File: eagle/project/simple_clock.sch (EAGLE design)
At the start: 7 parts, among them IC1 MAX7219CNG

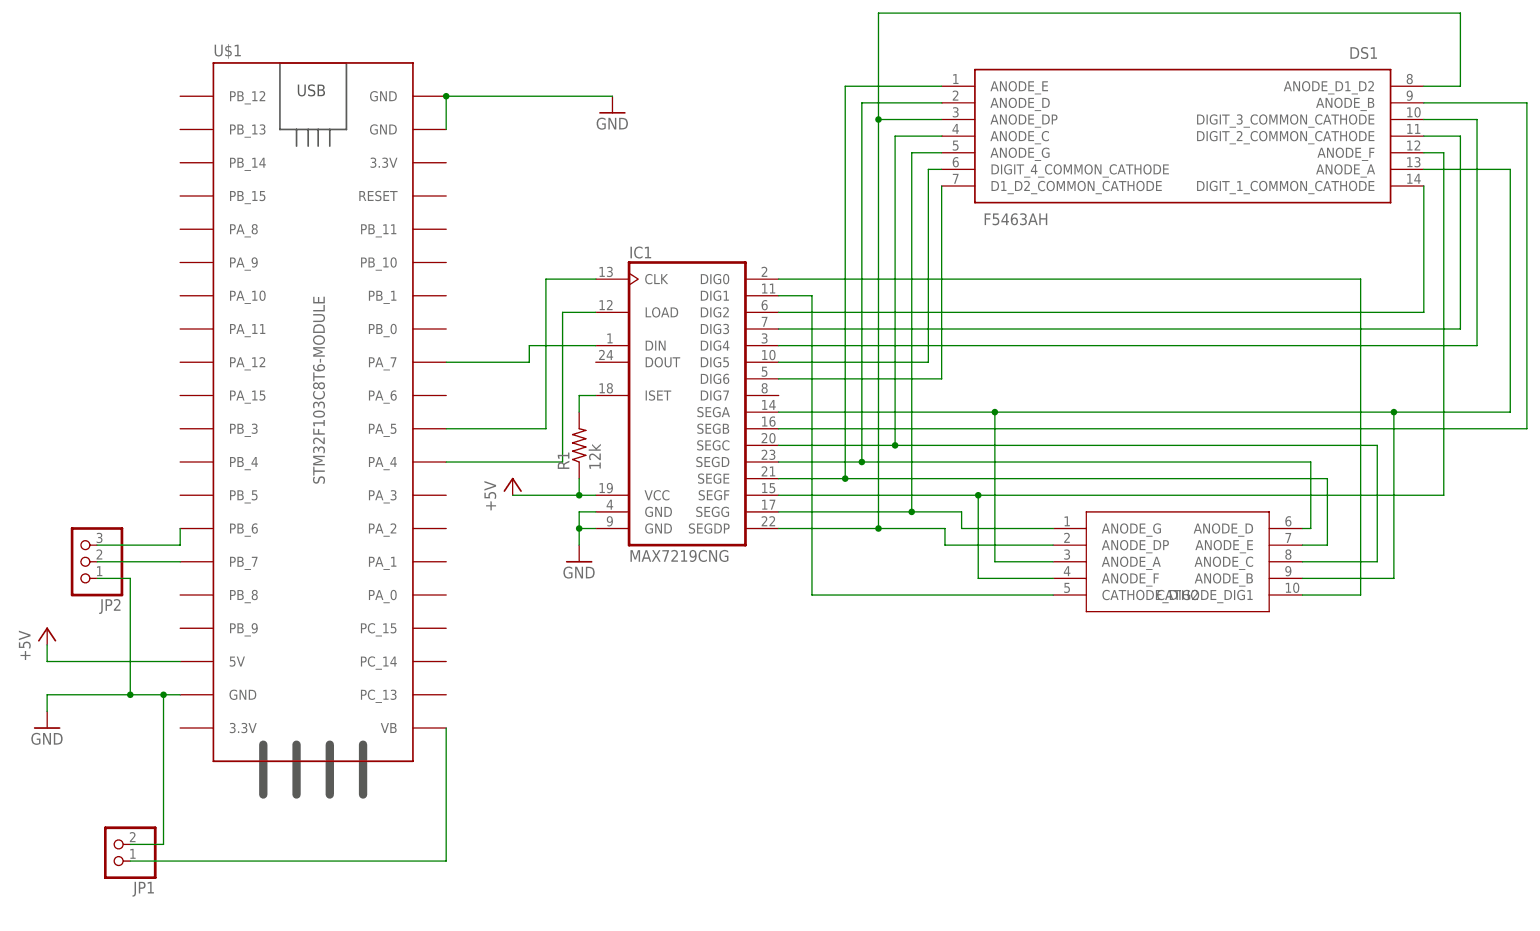
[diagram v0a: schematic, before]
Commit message: made pcb in Eagle
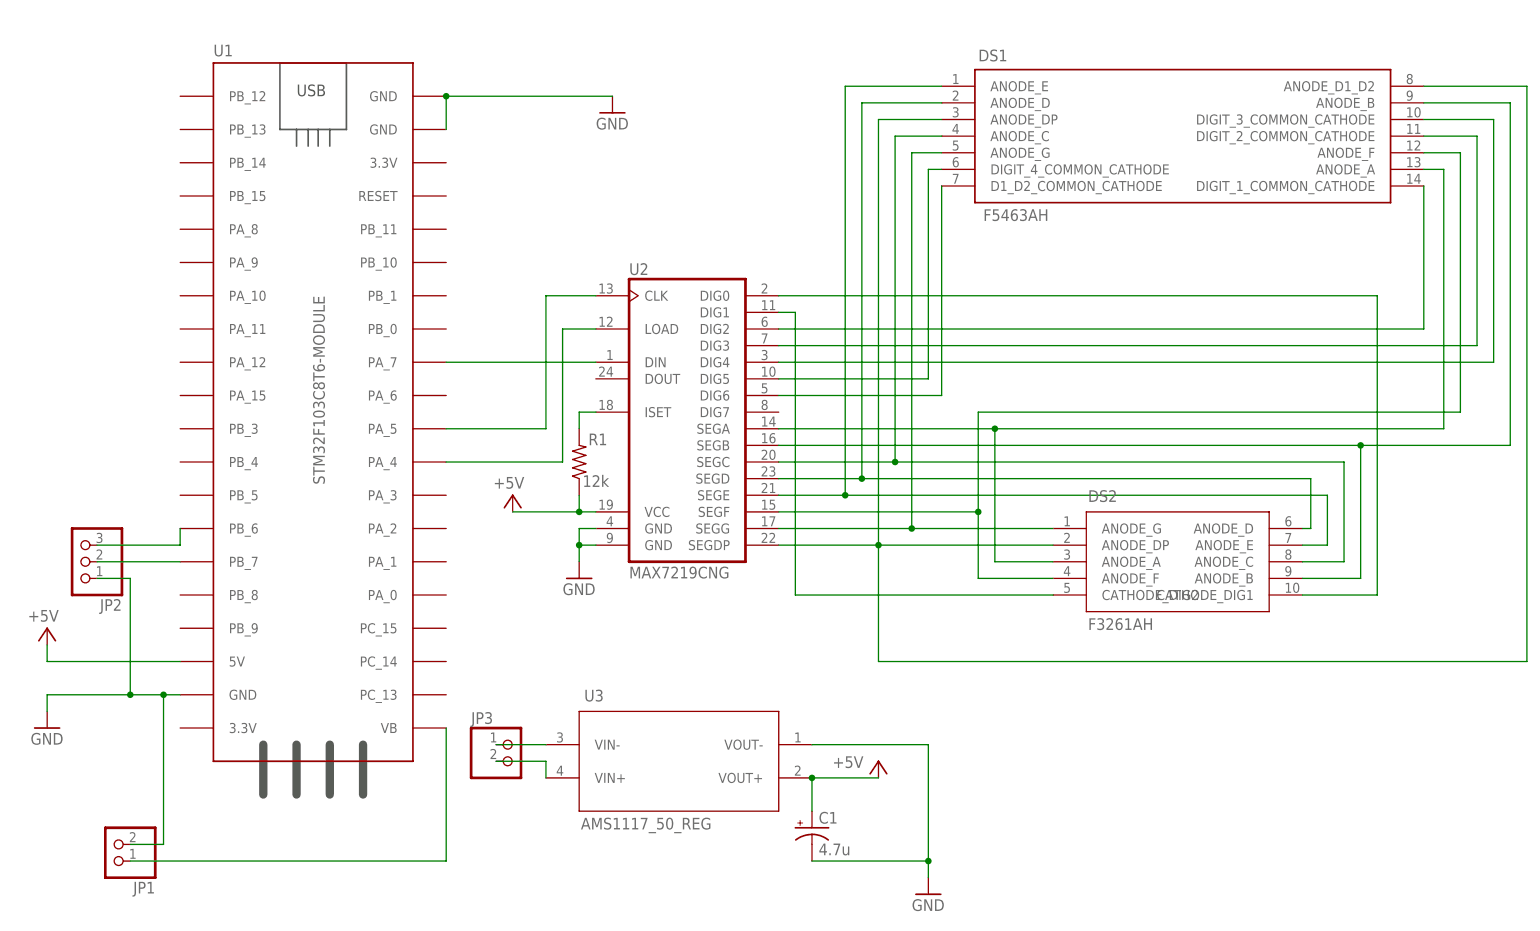
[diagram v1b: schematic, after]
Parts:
- removed IC1: MAX7219CNG, maxim:MAX7219CNG
- removed U$2: F3261AH, clock-7-seg:F3261AH
- added C1: 4.7u, rcl:CPOL-USE1.8-4
- added DS2: F3261AH, simple_clock:F3261AH
- added JP3: (no value), pinhead:PINHD-1X2
- added U2: MAX7219CNG, maxim:MAX7219CNG
- added U3: AMS1117_50_REG, simple_clock:AMS1117_50_REG
- DS1: device clock-7-seg:F5463AH -> simple_clock:F5463AH
- renumbered U$1 to U1
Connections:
- removed net N$17: DS1.ANODE_D1_D2, DS1.ANODE_DP, IC1.SEGDP, U$2.ANODE_DP
- new net N$23: JP3.1, U3.VIN-
- new net N$24: JP3.2, U3.VIN+
- new net N$25: DS1.ANODE_B, DS2.ANODE_B, U2.SEGB
- net +5V: now also C1.+, U2.VCC, U3.VOUT+; no longer IC1.VCC
- net GND: now also C1.-, U2.GND@1, U2.GND@2, U3.VOUT-; no longer IC1.GND@1, IC1.GND@2
- net N$1: now also U2.DIG4; no longer IC1.DIG4
- net N$10: now also U2.LOAD; no longer IC1.LOAD
- net N$11: now also DS2.ANODE_A, U2.SEGA; no longer IC1.SEGA, U$2.ANODE_A, U$2.ANODE_B
- net N$12: now also DS2.ANODE_E, U2.SEGE; no longer IC1.SEGE, U$2.ANODE_E
- net N$13: now also DS1.ANODE_D1_D2, DS1.ANODE_DP, DS2.ANODE_DP, U2.SEGDP; no longer DS1.ANODE_B, IC1.SEGB
- net N$14: now also DS2.ANODE_F, U2.SEGF; no longer IC1.SEGF, U$2.ANODE_F
- net N$15: now also DS2.ANODE_C, U2.SEGC; no longer IC1.SEGC, U$2.ANODE_C
- net N$16: now also DS2.ANODE_D, U2.SEGD; no longer IC1.SEGD, U$2.ANODE_D
- net N$18: now also DS2.ANODE_G, U2.SEGG; no longer IC1.SEGG, U$2.ANODE_G
- net N$19: now also U2.ISET; no longer IC1.ISET
- net N$2: now also U2.DIG6; no longer IC1.DIG6
- net N$3: now also U2.DIN; no longer IC1.DIN
- net N$4: now also U2.DIG2; no longer IC1.DIG2
- net N$5: now also DS2.CATHODE_DIG1, U2.DIG0; no longer IC1.DIG0, U$2.CATHODE_DIG1
- net N$6: now also DS2.CATHODE_DIG2, U2.DIG1; no longer IC1.DIG1, U$2.CATHODE_DIG2
- net N$7: now also U2.DIG3; no longer IC1.DIG3
- net N$8: now also U2.DIG5; no longer IC1.DIG5
- net N$9: now also U2.CLK; no longer IC1.CLK
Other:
- moved on the sheet: R1

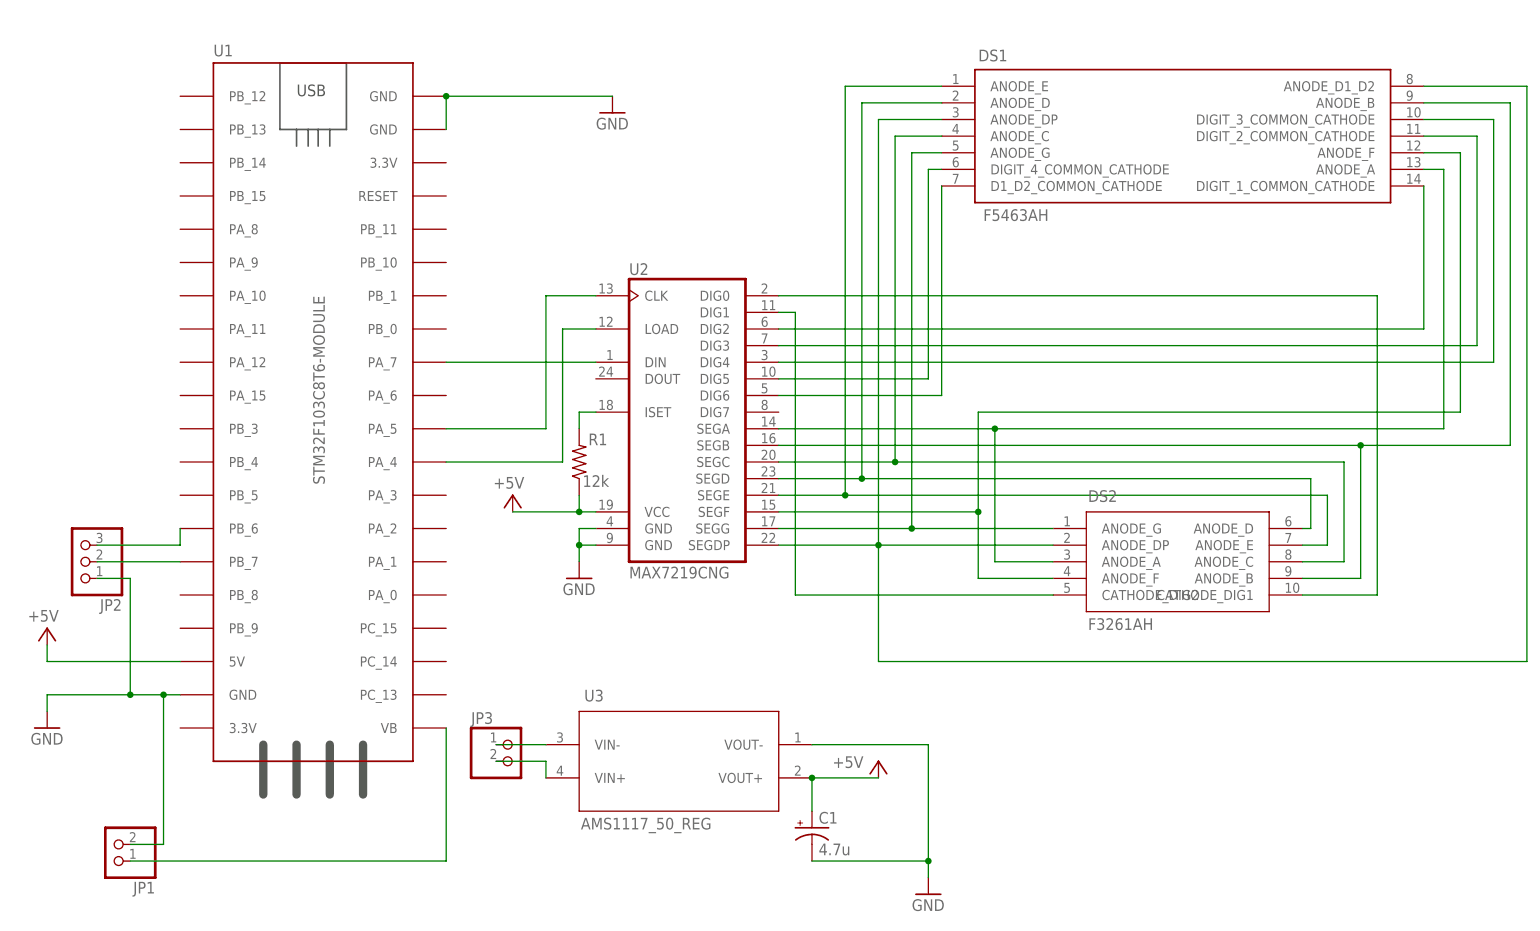
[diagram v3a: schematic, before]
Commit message: updated footprints
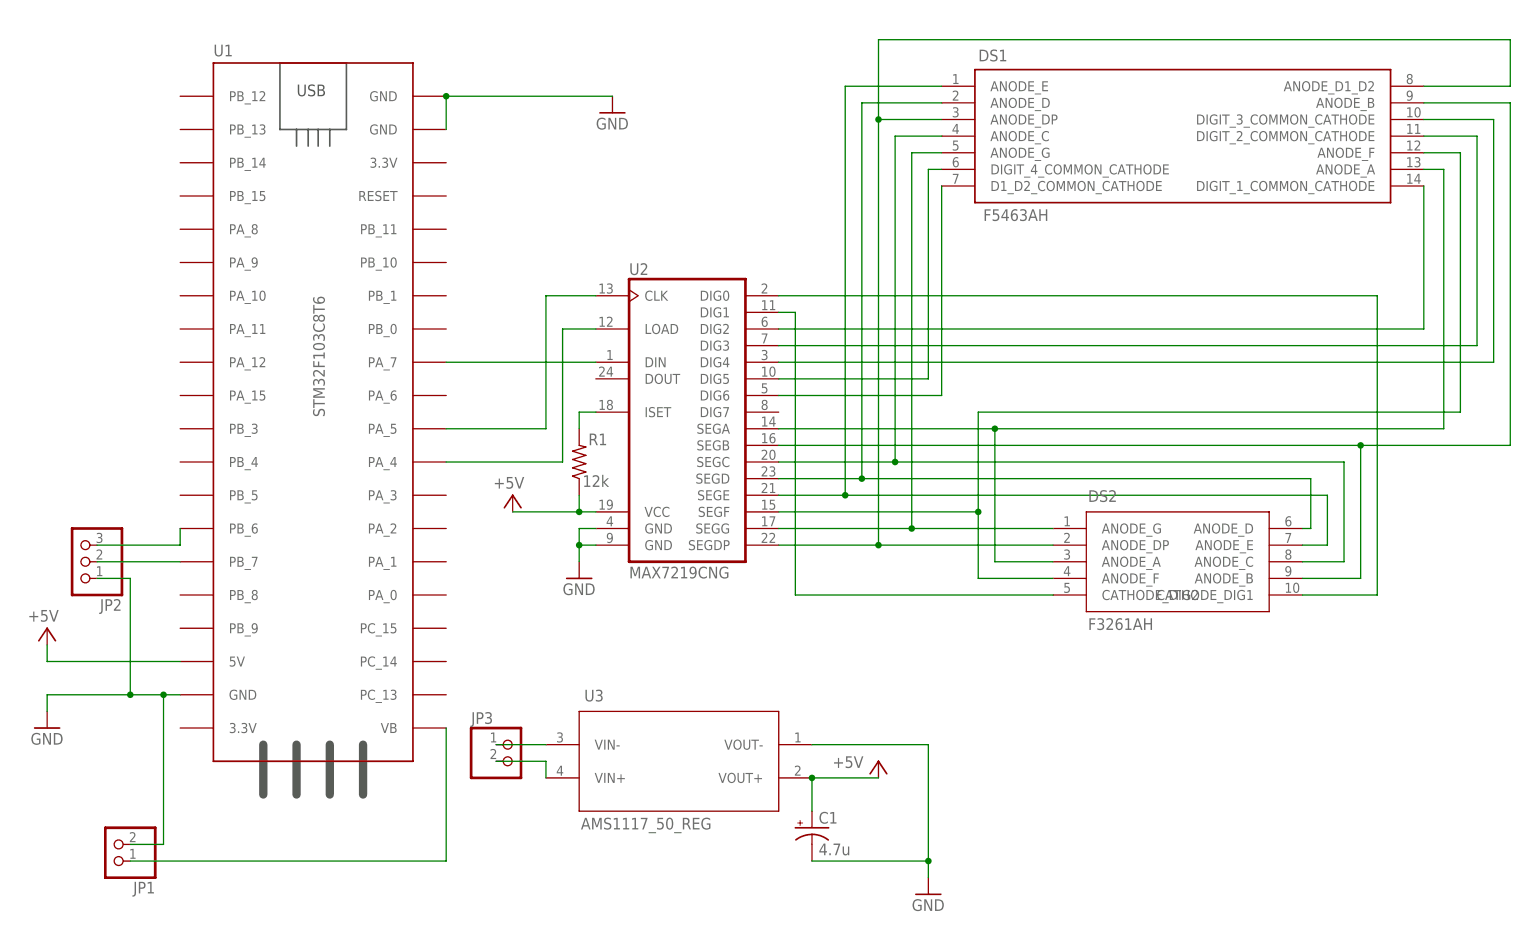
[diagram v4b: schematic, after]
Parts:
- U1: value STM32F103C8T6-MODULE -> STM32F103C8T6; device stm32f103c8t6_module:STM32F103C8T6-MODULE -> stm32f103c8t6_module:STM32F103C8T6
